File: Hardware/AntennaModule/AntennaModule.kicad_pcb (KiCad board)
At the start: 4 copper layers, 80 x 80 mm, 53 parts, among them J1 Conn_01x10, SW1 ColdStart, U1 C0727J5003AHF-1, U2 C0727J5003AHF-1, U3 NJG1155UX2, U4 NT1192FAAE1S, U5 PD0922J5050S2HF, U6 NT1192FAAE1S, U7 NEO-D9C, U8 NEO-F9P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

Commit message: 配線中
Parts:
- moved C3 1.62 mm to (161.2, 91.0)
- moved R2 1.50 mm to (150.8, 111.2)
- moved U2 1.50 mm to (150.0, 109.3)
- moved L1 1.30 mm to (162.7, 88.8)
- moved U3 1.28 mm to (162.7, 90.5)
- moved C8 1.13 mm to (162.8, 100.9)
- moved X2 1.06 mm to (164.4, 96.8)
- moved L4 1.03 mm to (163.3, 99.5)
- moved D4 0.97 mm to (156.3, 108.2), turned to 90 degrees
- moved D5 0.97 mm to (143.7, 108.2), turned to -90 degrees
- moved L5 0.95 mm to (167.1, 96.8)
- moved L3 0.86 mm to (163.3, 94.2)
- moved C5 0.86 mm to (168.5, 97.3)
- moved C7 0.80 mm to (163.7, 92.8)
- moved U8 0.66 mm to (178.6, 90.9)
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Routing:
- net Net-(U2-Input): track 0.64 -> 20.3 mm
- net +3.3VA: track 0.00 -> 9.80 mm
- net Net-(AE1B-LB2): track 0.00 -> 2.31 mm
- net Net-(AE1B-LB1): track 0.00 -> 2.31 mm
- net Net-(U5-Output2): track 0.00 -> 2.29 mm
- net Net-(AE1A-HB2): track 0.00 -> 2.21 mm
- net Net-(AE1A-HB1): track 0.00 -> 2.21 mm
- net +3.3VP: track 0.00 -> 2.04 mm
- net Net-(U4-RFOUT): track 0.00 -> 1.27 mm
- net Net-(U3-RFOUT): track 0.00 -> 1.02 mm
- net Net-(U1-Input): track 0.63 -> 0.00 mm
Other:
- board text added: "上カプラは25milグリッドから0.0025mm下にずれてる"

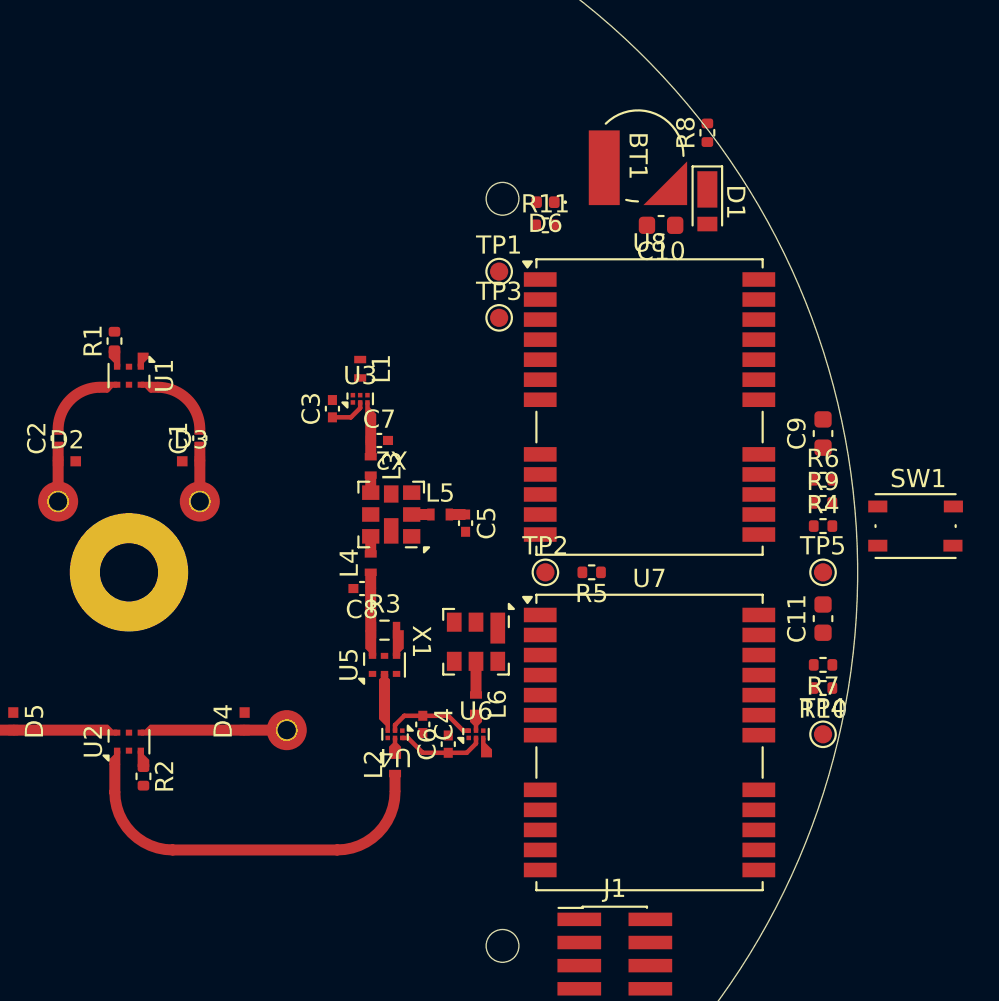
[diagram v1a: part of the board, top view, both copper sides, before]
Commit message: RFフロントエンド配線完了
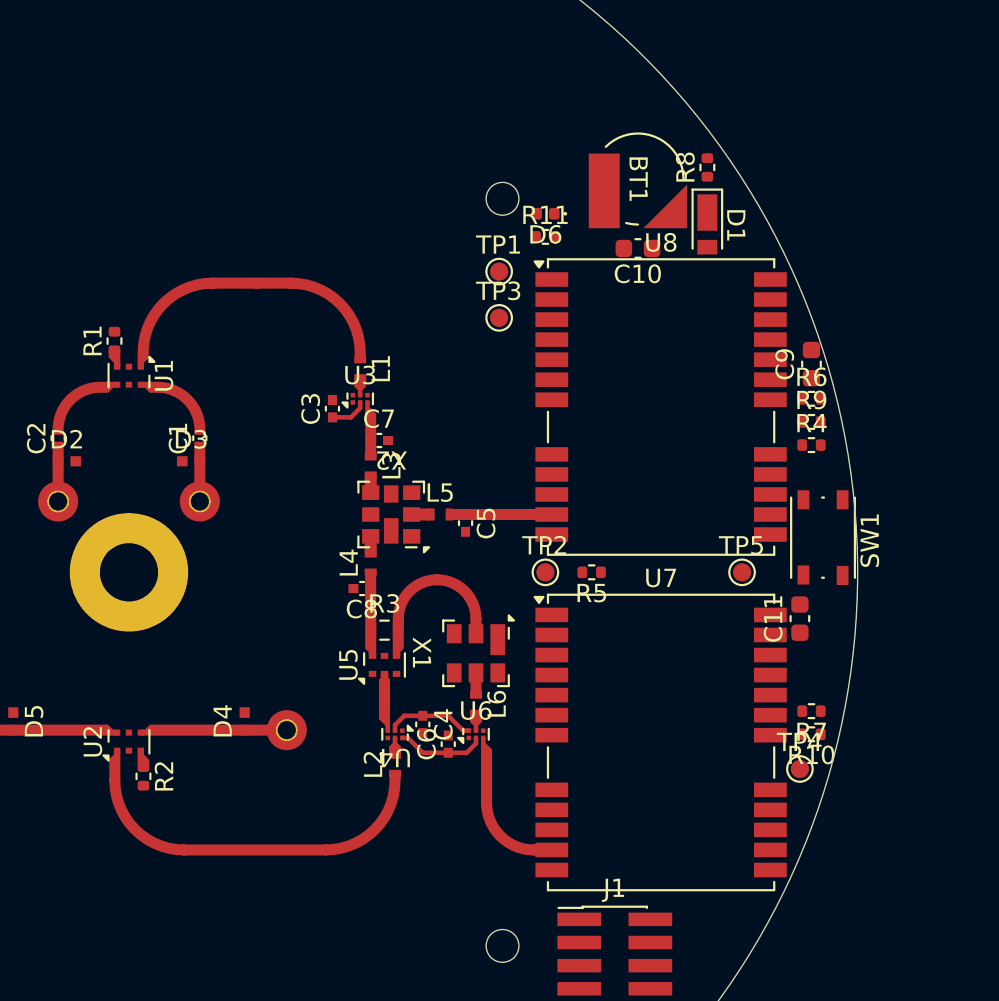
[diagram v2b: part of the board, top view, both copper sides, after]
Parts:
- moved SW1 5.12 mm to (188.1, 98.1), turned to -90 degrees
- moved R6 4.49 mm to (187.5, 90.5)
- moved R4 4.49 mm to (187.5, 93.0)
- moved R9 4.49 mm to (187.5, 91.7)
- moved TP5 4.44 mm to (183.7, 100.0)
- moved C9 3.86 mm to (187.5, 88.6)
- moved R10 2.62 mm to (187.5, 108.9)
- moved R7 2.62 mm to (187.5, 107.6)
- moved TP4 2.29 mm to (186.8, 110.8)
- moved R8 1.91 mm to (181.8, 77.8)
- moved C10 1.80 mm to (177.9, 82.2)
- moved BT1 1.27 mm to (177.9, 78.4)
- moved D1 1.27 mm to (181.8, 81.0)
- moved C11 1.27 mm to (186.8, 102.5)
- moved U7 0.64 mm to (179.2, 109.3)
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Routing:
- net Net-(U1-Input): track 0.00 -> 16.0 mm
- net Net-(U5-Output1): track 0.00 -> 7.99 mm
- net /RF_IN_D9C: track 0.00 -> 7.44 mm
- net /RF_IN_F9P: track 0.00 -> 4.73 mm
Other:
- board text added: "↓ここは50Ωじゃなくてもいいので0.66mm"
- board text added: "ここは50Ωなので0.605mm↗"
- board text added: "曲げ半径は配線幅の3倍以上 抵抗の中心xは接続するパッドの中心xから外側に0.145オフセット 上カプラは25milグリッドから0.0025mm下にずれてる -(0.605-0.35)/2 カプラのパッドX位置から伝送線路X位置のオフセット RFINパッドの高さは25milグリッド揃え"
- board text added: "電源リターンパス"
- board text removed: "-(0.605-0.35)/2 カプラのパッドX位置から伝送線路X位置のオフセット"
- board text removed: "RFINパッドの高さを揃える"
- board text removed: "上カプラは25milグリッドから0.0025mm下にずれてる"
- board text removed: "曲げ半径は配線幅の3倍以上 抵抗の中心xは接続するパッドの中心xから外側に0.145オフセット 下側TVSダイオード位置合わせ済"

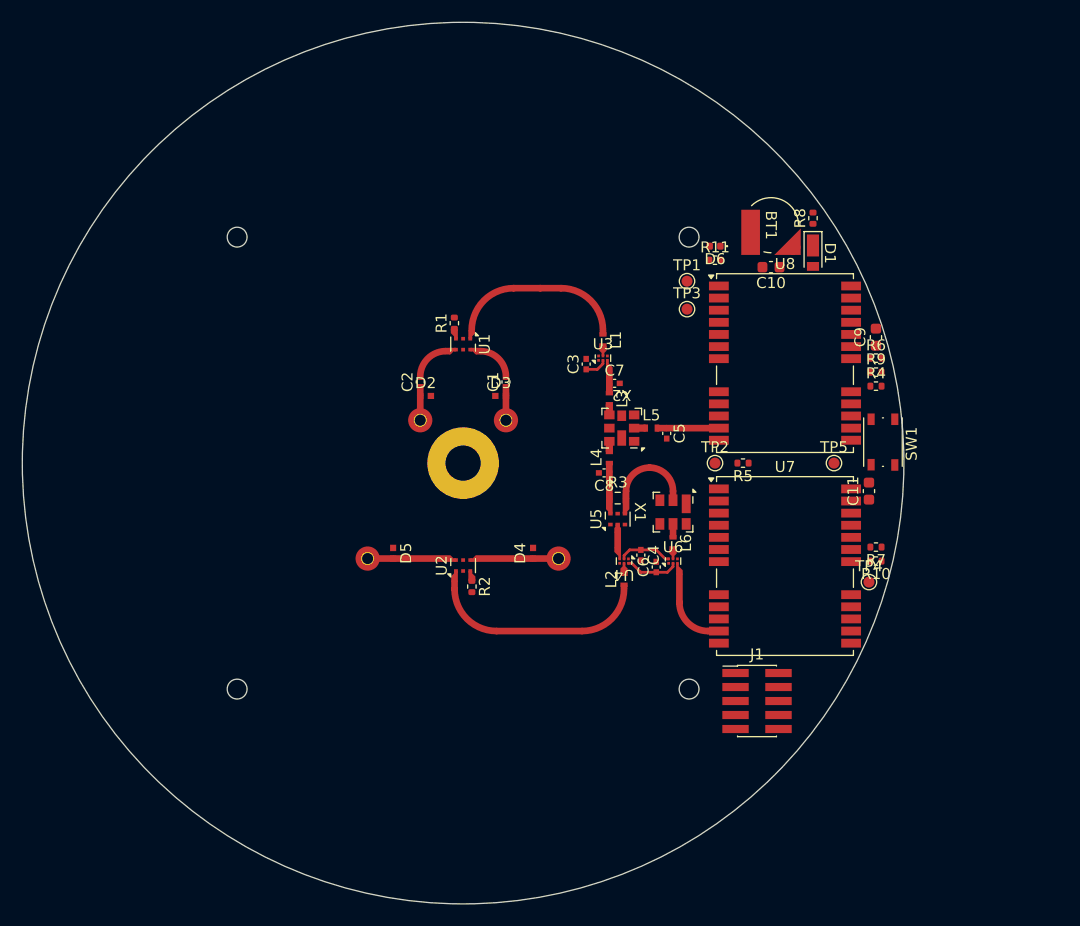
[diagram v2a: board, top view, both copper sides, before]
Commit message: add GND plane
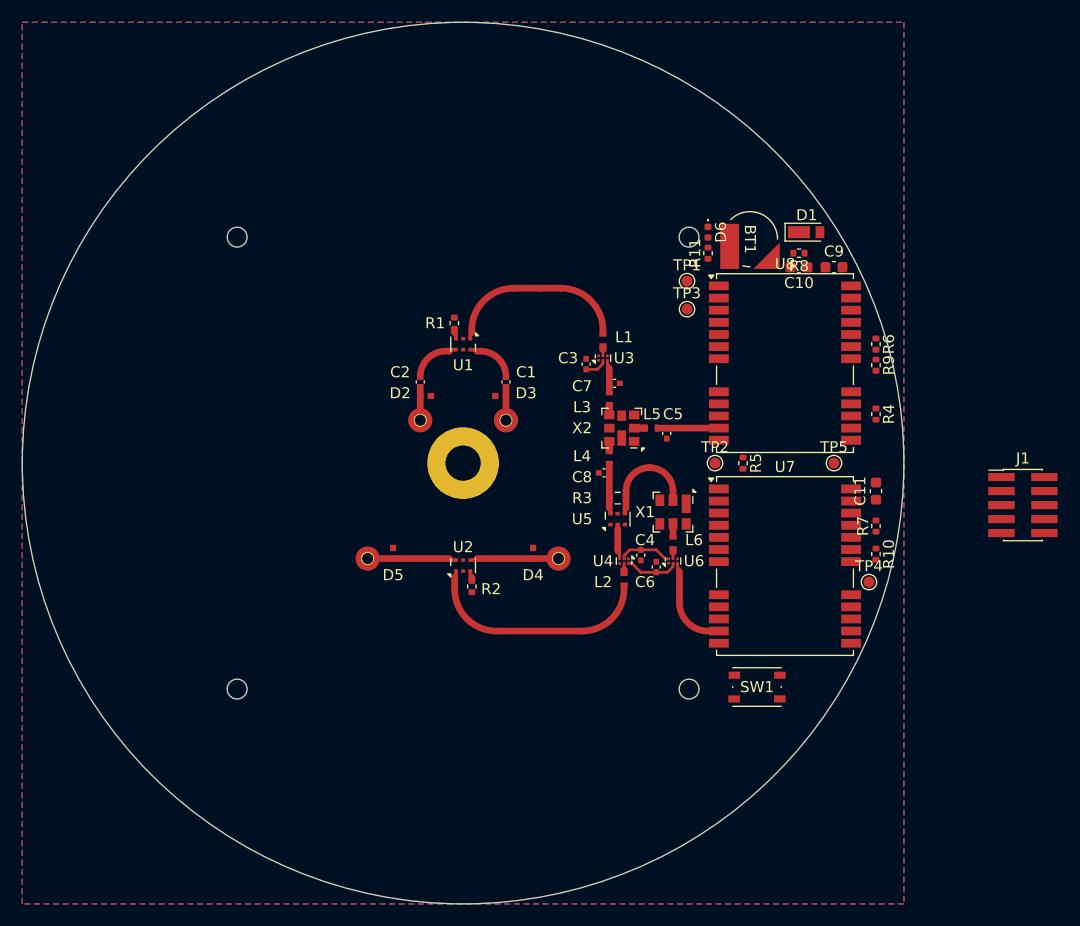
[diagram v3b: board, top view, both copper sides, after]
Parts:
- moved J1 30.0 mm to (200.8, 103.8)
- moved SW1 25.0 mm to (176.7, 120.3), turned to 180 degrees
- moved C9 7.41 mm to (183.7, 82.2), turned to 0 degrees
- moved R8 3.42 mm to (180.5, 81.0), turned to 180 degrees
- moved R4 2.54 mm to (187.5, 95.6), turned to -90 degrees
- moved C10 2.54 mm to (180.5, 82.2)
- moved BT1 2.29 mm to (176.0, 79.7)
- moved D1 1.99 mm to (181.2, 79.0), turned to 0 degrees
- moved R7 1.91 mm to (187.5, 105.7), turned to 90 degrees
- moved D6 1.42 mm to (172.2, 79.0), turned to -90 degrees
- moved R6 1.27 mm to (187.5, 89.2), turned to -90 degrees
- moved R11 0.90 mm to (172.2, 81.0), turned to 90 degrees
- moved R10 0.64 mm to (187.5, 108.3), turned to -90 degrees
- moved R9 0.64 mm to (187.5, 91.1), turned to -90 degrees
- moved C11 0.63 mm to (187.5, 102.5)
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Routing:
- added copper zone on B.Cu, net GND
- added copper zone on F.Cu, net GND
- added copper zone on In1.Cu, net GND
- added copper zone on In2.Cu, net GND
